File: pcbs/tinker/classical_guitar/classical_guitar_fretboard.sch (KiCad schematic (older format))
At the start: 152 parts, among them U1 AT42QT1110-A, U2 AT42QT1110-A, U3 AT42QT1110-A

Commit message: Rearranged labels
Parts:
- renumbered Je2 to Je1, Je3 to Je2, Je1 to Je3
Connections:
- net Electrode1: now also JPe1.2 (C); no longer JPe11.2 (C)
- net Electrode10: now also JPe10.2 (C)
- net Electrode11: now also JPe11.2 (C); no longer JPe21.2 (C)
- net Electrode12: now also JPe12.2 (C); no longer JPe22.2 (C)
- net Electrode13: now also JPe13.2 (C); no longer JPe23.2 (C)
- net Electrode14: now also JPe14.2 (C); no longer JPe24.2 (C)
- net Electrode15: now also JPe15.2 (C); no longer JPe25.2 (C)
- net Electrode16: now also JPe16.2 (C); no longer JPe26.2 (C)
- net Electrode17: now also JPe17.2 (C); no longer JPe27.2 (C)
- net Electrode18: now also JPe18.2 (C); no longer JPe28.2 (C)
- net Electrode19: now also JPe19.2 (C); no longer JPe29.2 (C)
- net Electrode2: now also JPe2.2 (C); no longer JPe12.2 (C)
- net Electrode20: no longer JPe30.2 (C)
- net Electrode21: now also JPe21.2 (C); no longer JPe1.2 (C)
- net Electrode22: now also JPe22.2 (C); no longer JPe2.2 (C)
- net Electrode23: now also JPe23.2 (C); no longer JPe3.2 (C)
- net Electrode24: now also JPe24.2 (C); no longer JPe4.2 (C)
- net Electrode25: now also JPe25.2 (C); no longer JPe5.2 (C)
- net Electrode26: now also JPe26.2 (C); no longer JPe6.2 (C)
- net Electrode27: now also JPe27.2 (C); no longer JPe7.2 (C)
- net Electrode28: now also JPe28.2 (C); no longer JPe8.2 (C)
- net Electrode29: now also JPe29.2 (C); no longer JPe9.2 (C)
- net Electrode3: now also JPe3.2 (C); no longer JPe13.2 (C)
- net Electrode30: now also JPe30.2 (C); no longer JPe10.2 (C)
- net Electrode4: now also JPe4.2 (C); no longer JPe14.2 (C)
- net Electrode5: now also JPe5.2 (C); no longer JPe15.2 (C)
- net Electrode6: now also JPe6.2 (C); no longer JPe16.2 (C)
- net Electrode7: now also JPe7.2 (C); no longer JPe17.2 (C)
- net Electrode8: now also JPe8.2 (C); no longer JPe18.2 (C)
- net Electrode9: now also JPe9.2 (C); no longer JPe19.2 (C)
- net at JPe11.3 (B): now also Je2.1 (Pin_1); no longer Je1.1 (Pin_1)
- net at JPe12.3 (B): now also Je2.2 (Pin_2); no longer Je1.2 (Pin_2)
- net at JPe13.3 (B): now also Je2.3 (Pin_3); no longer Je1.3 (Pin_3)
- net at JPe14.3 (B): now also Je2.4 (Pin_4); no longer Je1.4 (Pin_4)
- net at JPe15.3 (B): now also Je2.5 (Pin_5); no longer Je1.5 (Pin_5)
- net at JPe16.3 (B): now also Je2.6 (Pin_6); no longer Je1.6 (Pin_6)
- net at JPe17.3 (B): now also Je2.7 (Pin_7); no longer Je1.7 (Pin_7)
- net at JPe18.3 (B): now also Je2.8 (Pin_8); no longer Je1.8 (Pin_8)
- net at JPe19.3 (B): now also Je2.9 (Pin_9); no longer Je1.9 (Pin_9)
- net at Je1.10 (Pin_10): now also JPe10.3 (B); no longer JPe20.3 (B)
- net at Je2.10 (Pin_10): now also JPe20.3 (B); no longer JPe30.3 (B)
- net at JPe21.3 (B): now also Je3.1 (Pin_1); no longer Je2.1 (Pin_1)
- net at JPe22.3 (B): now also Je3.2 (Pin_2); no longer Je2.2 (Pin_2)
- net at JPe23.3 (B): now also Je3.3 (Pin_3); no longer Je2.3 (Pin_3)
- net at JPe24.3 (B): now also Je3.4 (Pin_4); no longer Je2.4 (Pin_4)
- net at JPe25.3 (B): now also Je3.5 (Pin_5); no longer Je2.5 (Pin_5)
- net at JPe26.3 (B): now also Je3.6 (Pin_6); no longer Je2.6 (Pin_6)
- net at JPe27.3 (B): now also Je3.7 (Pin_7); no longer Je2.7 (Pin_7)
- net at JPe28.3 (B): now also Je3.8 (Pin_8); no longer Je2.8 (Pin_8)
- net at JPe29.3 (B): now also Je3.9 (Pin_9); no longer Je2.9 (Pin_9)
- net at Je3.10 (Pin_10): now also JPe30.3 (B); no longer JPe10.3 (B)
- net at JPe1.3 (B): now also Je1.1 (Pin_1); no longer Je3.1 (Pin_1)
- net at JPe2.3 (B): now also Je1.2 (Pin_2); no longer Je3.2 (Pin_2)
- net at JPe3.3 (B): now also Je1.3 (Pin_3); no longer Je3.3 (Pin_3)
- net at JPe4.3 (B): now also Je1.4 (Pin_4); no longer Je3.4 (Pin_4)
- net at JPe5.3 (B): now also Je1.5 (Pin_5); no longer Je3.5 (Pin_5)
- net at JPe6.3 (B): now also Je1.6 (Pin_6); no longer Je3.6 (Pin_6)
- net at JPe7.3 (B): now also Je1.7 (Pin_7); no longer Je3.7 (Pin_7)
- net at JPe8.3 (B): now also Je1.8 (Pin_8); no longer Je3.8 (Pin_8)
- net at JPe9.3 (B): now also Je1.9 (Pin_9); no longer Je3.9 (Pin_9)
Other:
- moved on the sheet: E1, E10, E11, E12, E13, E14, E15, E16, E17, E18, E19, E2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

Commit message: Rearranged labels 2 and positions
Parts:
- renumbered JP1 to JPch1, JP2 to JPch2, JP3 to JPch3, JPmiso2 to JPmiso1, JPmiso3 to JPmiso2, JPmiso1 to JPmiso3, JPmosi2 to JPmosi1, JPmosi3 to JPmosi2, JPmosi1 to JPmosi3, JPsck2 to JPsck1, JPsck3 to JPsck2, JPsck1 to JPsck3, Jalternative_spi2 to Jalternative_spi1, Jalternative_spi3 to Jalternative_spi2, Jalternative_spi1 to Jalternative_spi3, Jc1 to Jch1, Js1 to Jsync1, Rc1 to Rch1, U2 to U1, U3 to U2, U1 to U3
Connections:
- net Electrode27: now also Rs7.1
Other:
- note added: "We are assuming that the change is open drain\nthat has no internal pull-up. We will use 100k \nas the external pull-up, but this value may vary."
- moved on the sheet: Cs1, Cs10, Cs2, Cs3, Cs4, Cs5, Cs6, Cs7, Cs8, Cs9, E21, E22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

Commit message: Added 74HC138 footprint
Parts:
- added U? (x4): 74HC138, symbol Custom_74xx:74HC138
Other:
- note added: "[!] Double check to see if SS line\nrequires active low or high,\nbecause this outputs 1 low"
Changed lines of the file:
@@
+	1    0    0    -1
+$EndComp
+Text Notes 9700 3950 0    50   ~ 0
+[!] Double check to see if SS line\nrequires active low or high,\nbecause this outputs 1 low
+$Comp
+L Custom_74xx:74HC138 U?
+U 1 1 61CB38E3
+P 13350 8350
+F 0 "U?" H 13350 9117 50  0000 C CNN
+F 1 "74HC138" H 13350 9026 50  0000 C CNN
+F 2 "" H 13350 8350 50  0001 C CNN
+F 3 "" H 13350 8350 50  0001 L BNN
+	1    13350 8350
+	1    0    0    -1
+$EndComp
+$Comp
+L Custom_74xx:74HC138 U?
+U 1 1 61CB4064
+P 13350 9800
+F 0 "U?" H 13350 10567 50  0000 C CNN
+F 1 "74HC138" H 13350 10476 50  0000 C CNN
+F 2 "" H 13350 9800 50  0001 C CNN
+F 3 "" H 13350 9800 50  0001 L BNN
+	1    13350 9800
+	1    0    0    -1
+$EndComp
+$Comp
+L Custom_74xx:74HC138 U?
+U 1 1 61D0A5DE
+P 13350 5450
+F 0 "U?" H 13350 6217 50  0000 C CNN
+F 1 "74HC138" H 13350 6126 50  0000 C CNN
+F 2 "" H 13350 5450 50  0001 C CNN
+F 3 "" H 13350 5450 50  0001 L BNN
+	1    13350 5450
+	1    0    0    -1
+$EndComp
+$Comp
+L Custom_74xx:74HC138 U?
+U 1 1 61D0A5E4
+P 13350 6900
+F 0 "U?" H 13350 7667 50  0000 C CNN
+F 1 "74HC138" H 13350 7576 50  0000 C CNN
+F 2 "" H 13350 6900 50  0001 C CNN
+F 3 "" H 13350 6900 50  0001 L BNN
+	1    13350 6900
 	1    0    0    -1
 $EndComp

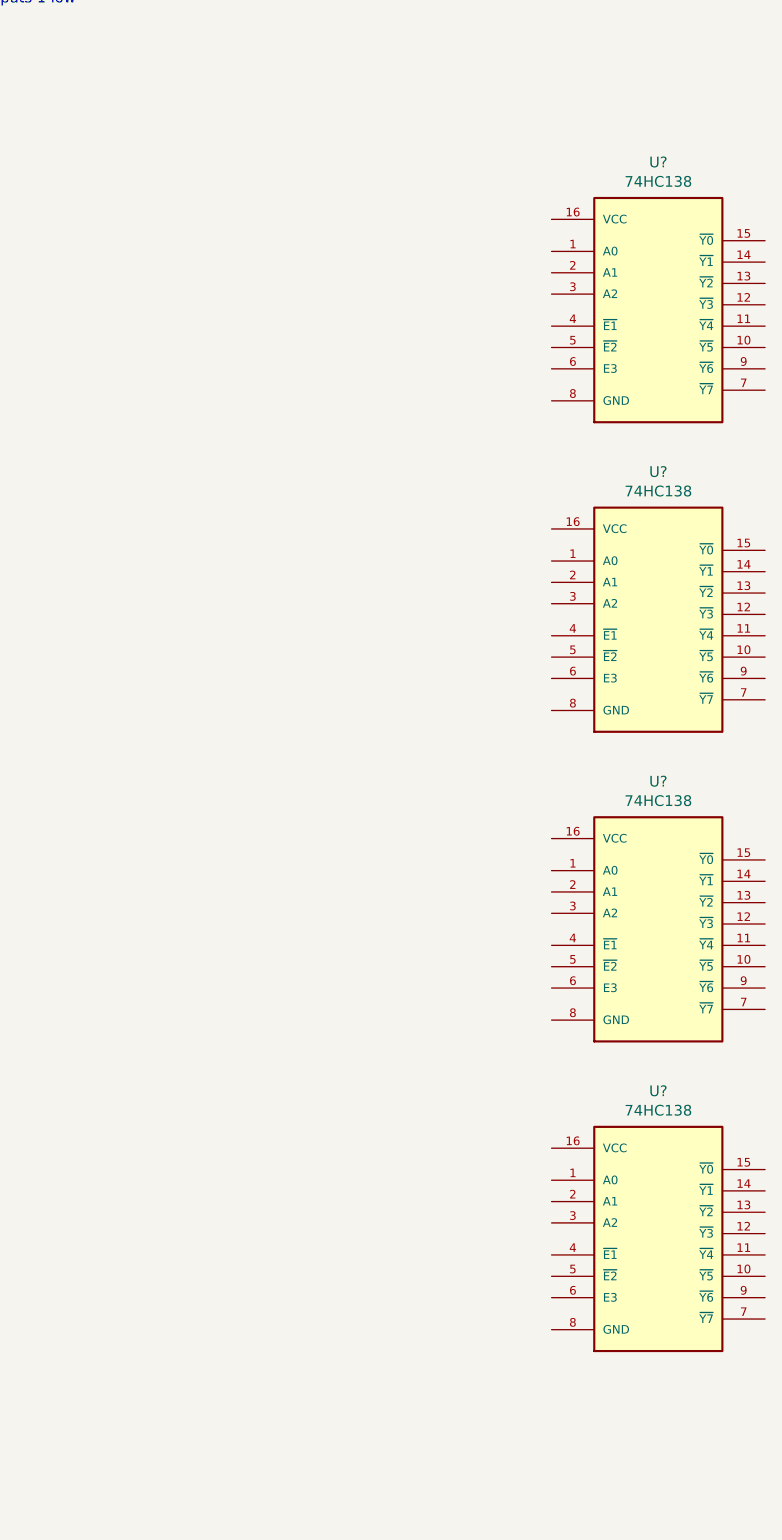
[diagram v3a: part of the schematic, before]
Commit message: Added decoders
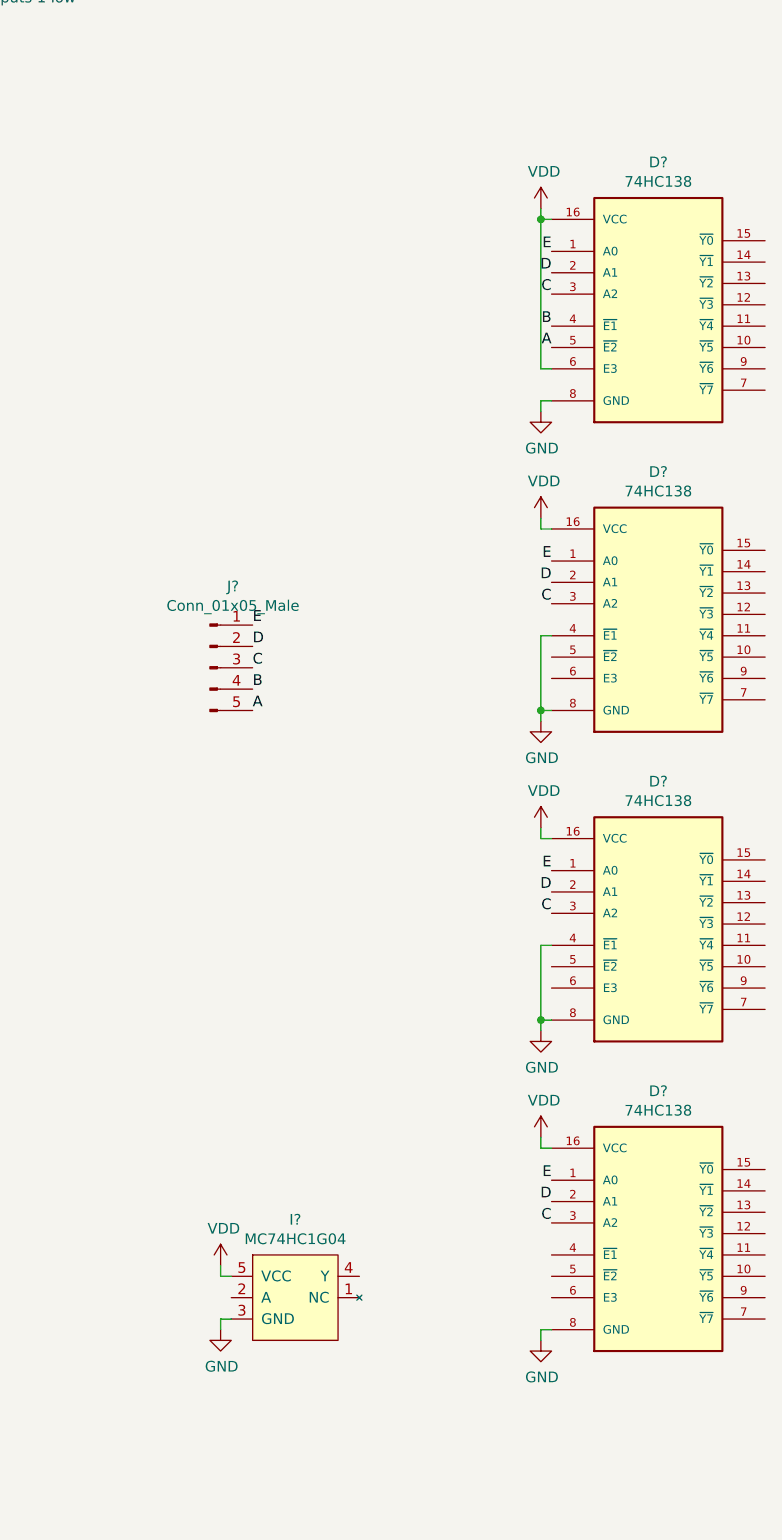
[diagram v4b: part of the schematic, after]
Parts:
- added I?: MC74HC1G04, symbol Custom_74xx:MC74HC1G04
- added J?: Conn_01x05_Male, symbol Connector:Conn_01x05_Male
- gave numbers to parts that had none: 1
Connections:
- net GND: now also D?.4 (~E1), D?.4 (~E1), D?.8 (GND), D?.8 (GND), D?.8 (GND), D?.8 (GND), I?.3 (GND)
- net VDD: now also D?.16 (VCC), D?.16 (VCC), D?.16 (VCC), D?.16 (VCC), D?.6 (E3), I?.5 (VCC)
- net E: now reaches D?.1 (A0)
- net E: now also D?.1 (A0), D?.1 (A0), D?.1 (A0), J?.1 (Pin_1)
- net D: now reaches D?.2 (A1)
- net D: now also D?.2 (A1), D?.2 (A1), D?.2 (A1), J?.2 (Pin_2)
- net C: now reaches D?.3 (A2)
- net C: now also D?.3 (A2), D?.3 (A2), D?.3 (A2), J?.3 (Pin_3)
- net B: now reaches D?.4 (~E1)
- net B: now also J?.4 (Pin_4)
- net A: now reaches D?.5 (~E2)
- net A: now also J?.5 (Pin_5)

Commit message: Established 5-to-32 decoder sheet
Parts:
- removed D? (x4): 74HC138, symbol Custom_74xx:74HC138
- removed I?: MC74HC1G04, symbol Custom_74xx:MC74HC1G04
- removed Jalternative_spi1, Jalternative_spi2, Jalternative_spi3: Conn_01x03_Male, symbol Connector:Conn_01x03_Male
- added Jalternative_spi1, Jalternative_spi2, Jalternative_spi3: Conn_01x04_Male, symbol Connector:Conn_01x04_Male
- added Jdecoder_output1: Conn_02x16_Odd_Even, symbol Connector_Generic:Conn_02x16_Odd_Even
- gave numbers to parts that had none: 1
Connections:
- net ~SS1: now also Jalternative_spi1.4 (Pin_4)
- net ~SS2: now also Jalternative_spi2.4 (Pin_4)
- net ~SS3: now also Jalternative_spi3.4 (Pin_4)
- net at JPmosi1.3 (B): now also Jalternative_spi1.1 (Pin_1)
- net at JPmiso1.3 (B): now also Jalternative_spi1.2 (Pin_2)
- net at JPsck1.3 (B): now also Jalternative_spi1.3 (Pin_3)
- net at JPsck2.3 (B): now also Jalternative_spi2.3 (Pin_3)
- net at JPmosi2.3 (B): now also Jalternative_spi2.1 (Pin_1)
- net at JPmiso2.3 (B): now also Jalternative_spi2.2 (Pin_2)
- net at JPmosi3.3 (B): now also Jalternative_spi3.1 (Pin_1)
- net at JPmiso3.3 (B): now also Jalternative_spi3.2 (Pin_2)
- net at JPsck3.3 (B): now also Jalternative_spi3.3 (Pin_3)
- new net ~OSS1: Jdecoder_output1.1 (Pin_1)
- new net ~OSS10: Jdecoder_output1.10 (Pin_10)
- new net ~OSS11: Jdecoder_output1.11 (Pin_11)
- new net ~OSS12: Jdecoder_output1.12 (Pin_12)
- new net ~OSS13: Jdecoder_output1.13 (Pin_13)
- new net ~OSS14: Jdecoder_output1.14 (Pin_14)
- new net ~OSS15: Jdecoder_output1.15 (Pin_15)
- new net ~OSS16: Jdecoder_output1.16 (Pin_16)
- new net ~OSS17: Jdecoder_output1.17 (Pin_17)
- new net ~OSS18: Jdecoder_output1.18 (Pin_18)
- new net ~OSS19: Jdecoder_output1.19 (Pin_19)
- new net ~OSS2: Jdecoder_output1.2 (Pin_2)
- new net ~OSS20: Jdecoder_output1.20 (Pin_20)
- new net ~OSS21: Jdecoder_output1.21 (Pin_21)
- new net ~OSS22: Jdecoder_output1.22 (Pin_22)
- new net ~OSS23: Jdecoder_output1.23 (Pin_23)
- new net ~OSS24: Jdecoder_output1.24 (Pin_24)
- new net ~OSS25: Jdecoder_output1.25 (Pin_25)
- new net ~OSS26: Jdecoder_output1.26 (Pin_26)
- new net ~OSS27: Jdecoder_output1.27 (Pin_27)
- new net ~OSS28: Jdecoder_output1.28 (Pin_28)
- new net ~OSS29: Jdecoder_output1.29 (Pin_29)
- new net ~OSS3: Jdecoder_output1.3 (Pin_3)
- new net ~OSS30: Jdecoder_output1.30 (Pin_30)
- new net ~OSS31: Jdecoder_output1.31 (Pin_31)
- new net ~OSS32: Jdecoder_output1.32 (Pin_32)
- new net ~OSS4: Jdecoder_output1.4 (Pin_4)
- new net ~OSS5: Jdecoder_output1.5 (Pin_5)
- new net ~OSS6: Jdecoder_output1.6 (Pin_6)
- new net ~OSS7: Jdecoder_output1.7 (Pin_7)
- new net ~OSS8: Jdecoder_output1.8 (Pin_8)
- new net ~OSS9: Jdecoder_output1.9 (Pin_9)
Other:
- note added: "The 32 outputs would connect to the ~SS~ pins"
- moved on the sheet: Cs1, Cs10, Cs11, Cs12, Cs13, Cs14, Cs15, Cs16, Cs17, Cs18, Cs19, Cs2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

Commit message: Rearranging schematic
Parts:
- added D3: GREEN, LED_SMD:LED_0603_1608Metric, symbol Device:LED_Small
- added Jbarrel1: Barrel_Jack_Switch, Connector_BarrelJack:BarrelJack_Horizontal, symbol Connector:Barrel_Jack_Switch
- added Jusb1: USB_B_Micro, Connector_USB:USB_Micro-B_Amphenol_10118194_Horizontal, symbol Connector:USB_B_Micro
- added R6: 1k5, Resistor_SMD:R_0603_1608Metric, symbol Device:R_Small
- added Rs31, Rs32, Rs33, Rs34, Rs35, Rs36, Rs37, Rs38, Rs39: 0k, symbol Device:R_Small
- Jalternative_spi1, Jalternative_spi2, Jalternative_spi3, Jpower1: footprint (none) -> Connector_PinSocket_2.54mm:PinSocket_1x04_P2.54mm_Vertical
- Jch1, Jcommon_spi1: footprint (none) -> Connector_PinSocket_2.54mm:PinSocket_1x03_P2.54mm_Vertical
- Jdecoder_input1: footprint (none) -> Connector_PinSocket_2.54mm:PinSocket_1x05_P2.54mm_Vertical
- Jdecoder_output1: footprint (none) -> Connector_PinSocket_2.54mm:PinSocket_2x16_P2.54mm_Vertical
- Je1, Je2, Je3: footprint (none) -> Connector_PinSocket_2.54mm:PinSocket_1x10_P2.54mm_Vertical
- Jsync1: footprint (none) -> Connector_PinSocket_2.54mm:PinSocket_1x01_P2.54mm_Vertical
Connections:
- net GND: now also Jbarrel1.2, Jbarrel1.3, Jusb1.5 (GND), R6.2
- net Sync1: now also Rs37.2; no longer Jsync1.1 (Pin_1), U2.31 (SYNC/SNS10K), U3.31 (SYNC/SNS10K)
- net VDD: now also D3.2 (A), Rs34.2, Rs35.2, Rs36.2; no longer U1.29 (~RESET), U2.29 (~RESET), U3.29 (~RESET)
- net mp2359/VBattery: now also Jbarrel1.1
- net mp2359/VUSB: now also Jusb1.1 (VBUS)
- net ~SS1: now also Rs31.2; no longer Jalternative_spi1.4 (Pin_4)
- net ~SS2: now also Rs32.2; no longer Jalternative_spi2.4 (Pin_4)
- net ~SS3: now also Rs33.2; no longer Jalternative_spi3.4 (Pin_4)
- new net: Rs34.1, U1.29 (~RESET)
- new net: Jsync1.1 (Pin_1), Rs37.1, Rs38.1, Rs39.1
- new net: Jalternative_spi1.4 (Pin_4), Rs31.1
- new net: Jalternative_spi2.4 (Pin_4), Rs32.1
- new net: Jalternative_spi3.4 (Pin_4), Rs33.1
- new net: Rs35.1, U2.29 (~RESET)
- new net: Rs36.1, U3.29 (~RESET)
- new net: D3.1 (K), R6.1
- new net Sync2: Rs38.2, U2.31 (SYNC/SNS10K)
- new net Sync3: Rs39.2, U3.31 (SYNC/SNS10K)
- no-connect marks 3 -> 7
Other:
- note added: "SPI 5-to-32 decoder"
- note removed: "[!] Double check to see if SS line\nrequires active low or high,\nbecause this outputs 1 low"
- moved on the sheet: Cd1, Cd2, Cd3, Cd4, Cd5, Cd6, Cs1, Cs10, Cs11, Cs12, Cs13, Cs14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
